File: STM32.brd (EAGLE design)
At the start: 100 x 80 mm, 35 parts, among them Q1 8MHz

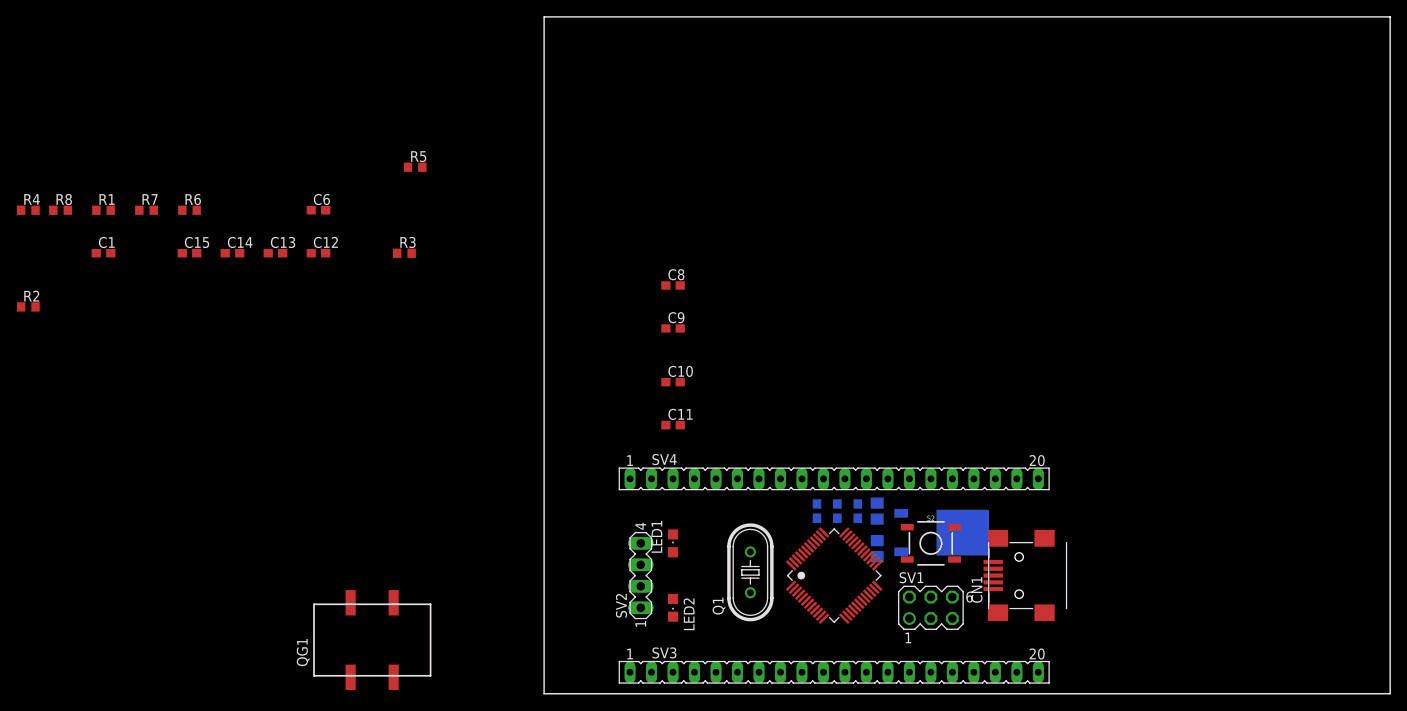
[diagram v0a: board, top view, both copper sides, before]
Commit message: V1.0
Se termina el primer ruteado
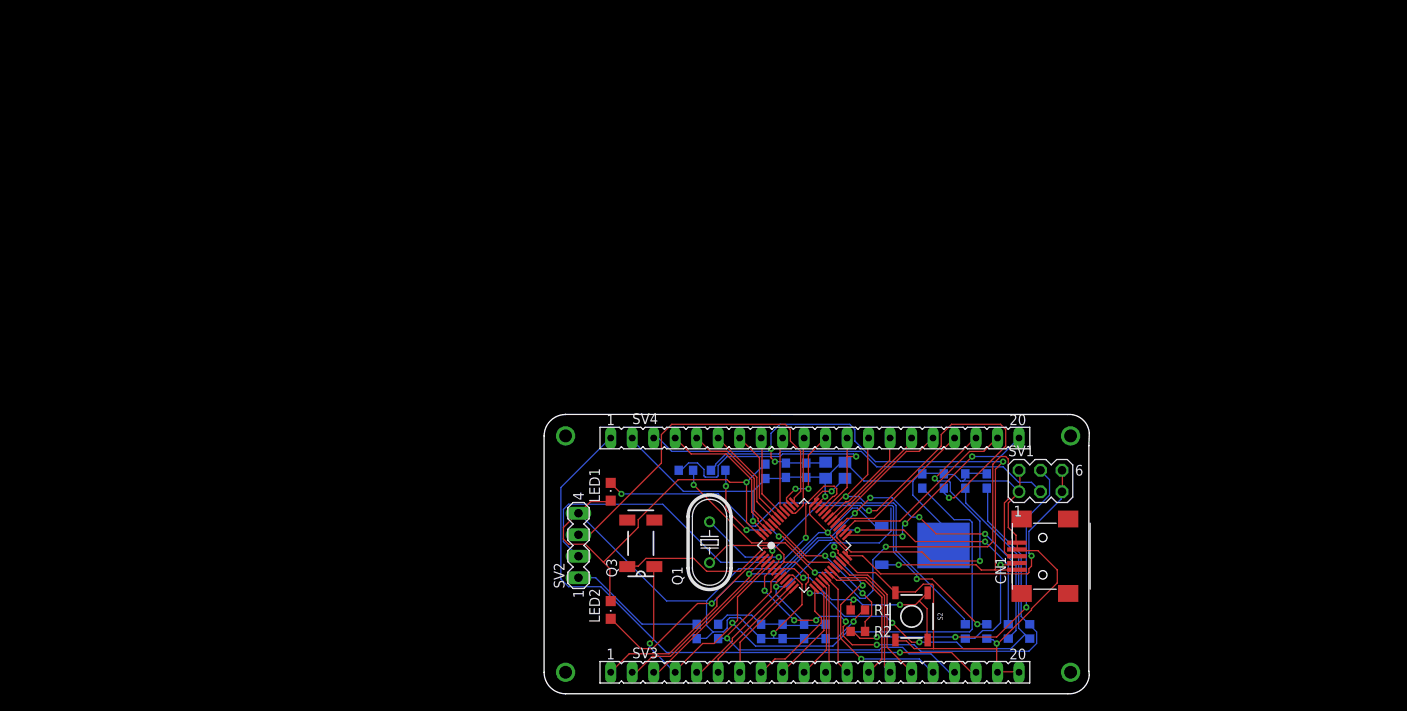
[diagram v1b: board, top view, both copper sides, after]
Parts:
- removed QG1: SG-615PCG, crystal:SG-615
- added Q3: MC-306, crystal:MC-306
- C12, C13, C14, C15: value 104 -> 20p
- moved R8 124.9 mm to (57.4, 7.37), flipped to the bottom, turned to 270 degrees
- moved R7 113.4 mm to (54.9, 7.37), flipped to the bottom, turned to 270 degrees
- moved R6 106.6 mm to (52.3, 7.37), flipped to the bottom, turned to 270 degrees
- moved R2 105.3 mm to (37.1, 7.37)
- moved R1 100.9 mm to (37.1, 9.91)
- moved C15 90.7 mm to (44.7, 25.1), flipped to the bottom, turned to 90 degrees
- moved C14 88.3 mm to (47.2, 25.1), flipped to the bottom, turned to 90 degrees
- moved C13 85.9 mm to (49.8, 25.1), flipped to the bottom, turned to 90 degrees
- moved C1 85.3 mm to (20.6, 7.37), flipped to the bottom, turned to 90 degrees
- moved R5 85.1 mm to (49.8, 7.37), flipped to the bottom, turned to 270 degrees
- moved R4 83.6 mm to (16.8, 26.4), flipped to the bottom, turned to 180 degrees
- moved C12 83.5 mm to (52.3, 25.1), flipped to the bottom, turned to 90 degrees
- moved C6 66.9 mm to (18.0, 7.37), flipped to the bottom, turned to 90 degrees
- moved R3 45.1 mm to (20.6, 26.4), flipped to the bottom
- moved C8 44.7 mm to (33.3, 7.37), flipped to the bottom, turned to 90 degrees
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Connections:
- removed net 5V: SV4.3
- removed net N$4: C12.2, C13.2
- removed net NRST: SV3.17
- removed net SWDCLK: SV2.3
- removed net SWDIO: SV2.2
- net +3V3: no longer QG1.4
- net +5V: now also SV4.3
- net GND: now also C12.2, C13.2; no longer QG1.2
- net OSC32IN: now also Q3.4; no longer QG1.3
- net OSC32OUT: now also Q3.1; no longer QG1.1
- net RESET: now also SV3.17
- net SWCLK: now also SV2.3
- net SWIO: now also SV2.2
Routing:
- net GND: track 0.00 -> 185.1 mm, vias 0 -> 5
- net +3V3: track 0.00 -> 184.9 mm, vias 0 -> 6
- net OSC32IN: track 0.00 -> 87.9 mm, vias 0 -> 3
- net +5V: track 0.00 -> 84.3 mm, vias 0 -> 4
- net OSC32OUT: track 0.00 -> 83.0 mm, vias 0 -> 2
- net VCC3V3: track 0.00 -> 72.8 mm, vias 0 -> 1
- net OSCIN: track 0.00 -> 72.7 mm, vias 0 -> 6
- net N$5: track 0.00 -> 71.9 mm, vias 0 -> 3
- net PC13: track 0.00 -> 69.1 mm, vias 0 -> 5
- net OSCOUT: track 0.00 -> 68.1 mm, vias 0 -> 3
- net RESET: track 0.00 -> 66.7 mm, vias 0 -> 4
- net N$7: track 0.00 -> 63.0 mm, vias 0 -> 3
- net N$3: track 0.00 -> 57.0 mm, vias 0 -> 3
- net SWIO: track 0.00 -> 51.1 mm, vias 0 -> 1
- net SWCLK: track 0.00 -> 42.1 mm
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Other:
- board size 100 x 80 mm -> 64.4 x 33 mm
